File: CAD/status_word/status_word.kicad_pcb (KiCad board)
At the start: 2 copper layers, 70 x 39 mm, 49 parts, among them J1 Conn_01x26_Pin, U1 74HC161, U2 74HC109, U3 74HC157, U4 74HC157, U5 74HC245, U6 74HC02

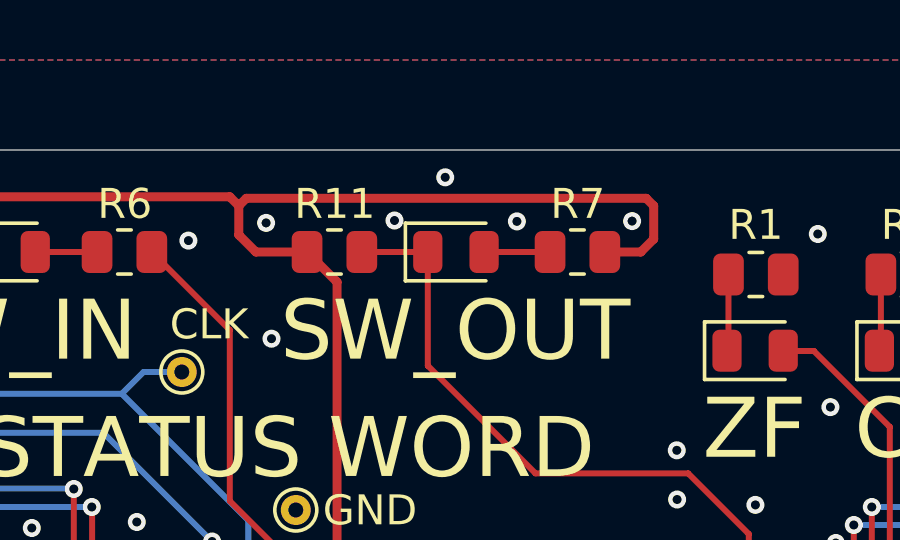
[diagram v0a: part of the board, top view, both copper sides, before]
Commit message: update SW, fix component rotations
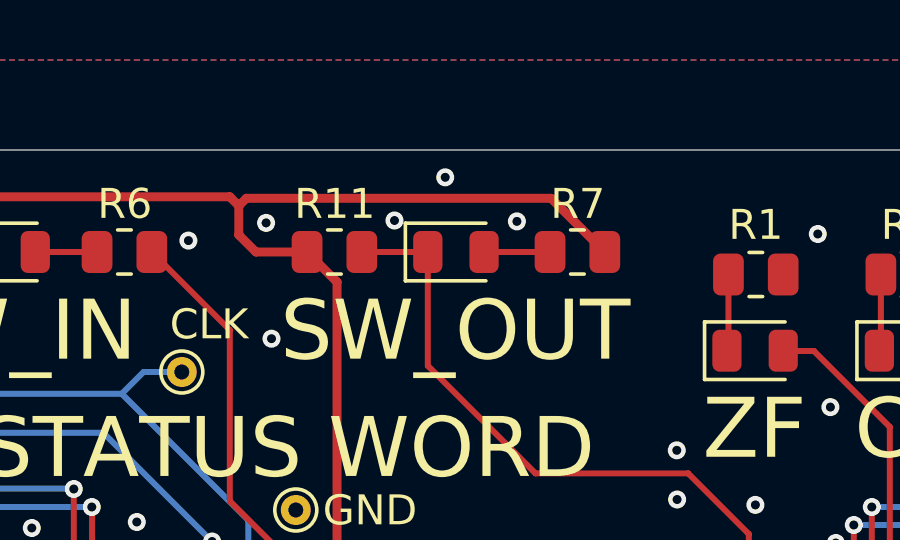
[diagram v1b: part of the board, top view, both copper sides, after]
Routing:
- net +5V: track 194.1 -> 190.2 mm
- net GND: vias 87 -> 86

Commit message: SW layout changes
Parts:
- TP2: moved to B.Cu
- turned TP2 to 180 degrees
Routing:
- net /sw.im: track 101.0 -> 100.0 mm
- net /sw.nf: track 84.3 -> 85.0 mm
- net /aflags.cf: track 27.6 -> 27.1 mm
- net /dbus3: track 62.6 -> 62.1 mm
- net GND: vias 86 -> 99

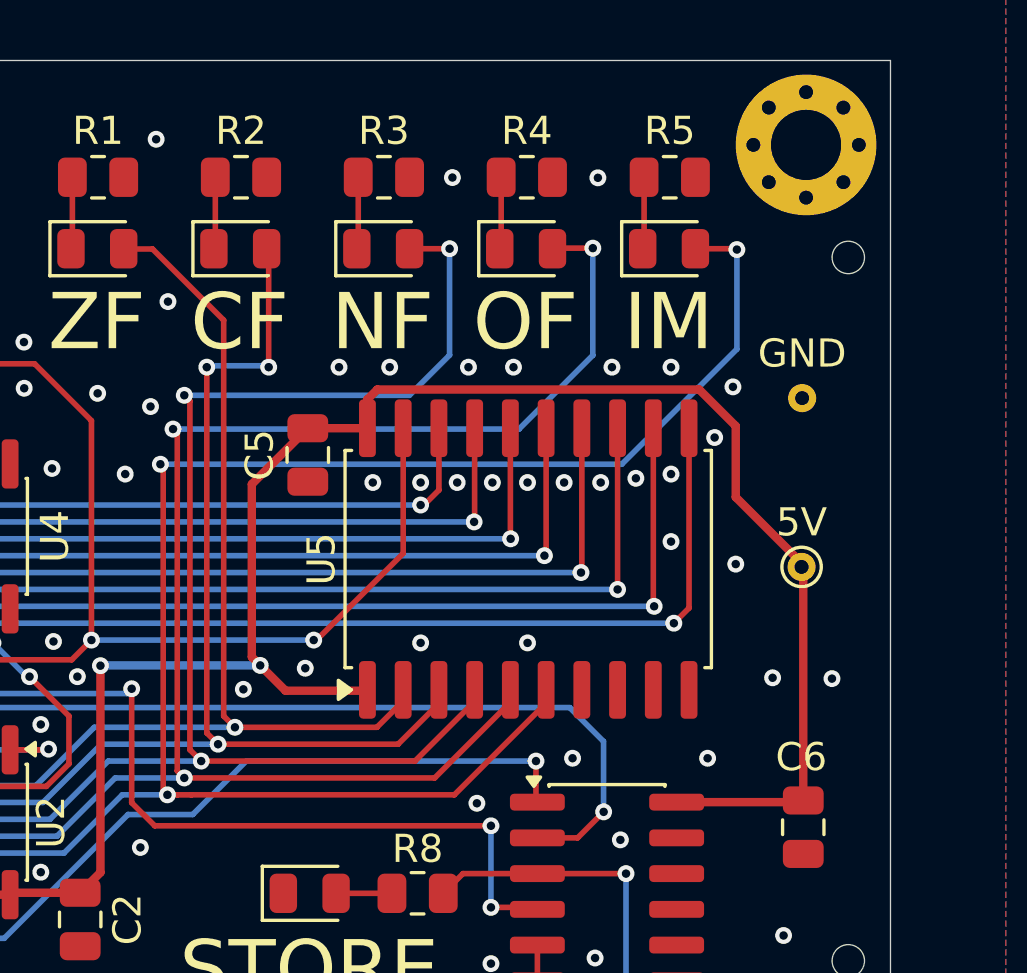
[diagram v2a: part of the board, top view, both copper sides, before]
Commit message: SW add keystone 5015 testpoint, small layout improvements
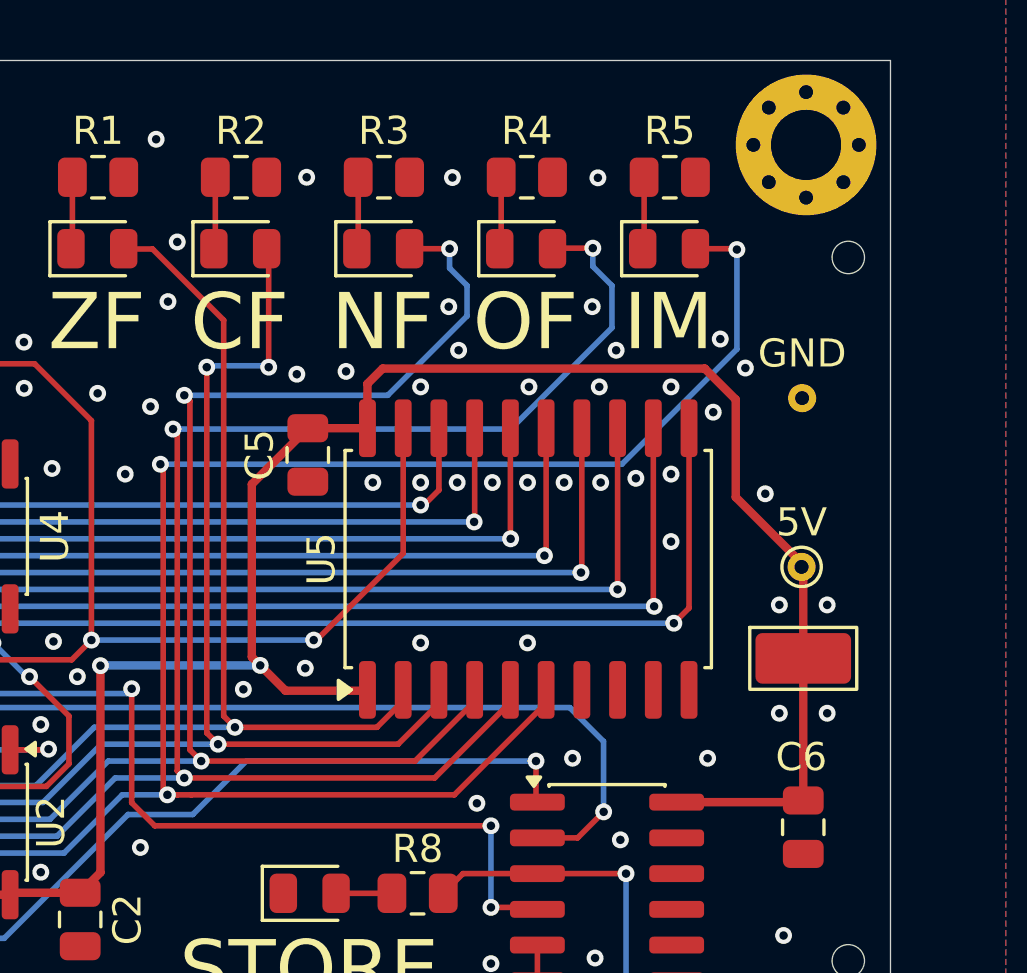
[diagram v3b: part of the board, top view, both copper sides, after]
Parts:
- added TP5: RH-5015, TestPoint:TestPoint_Keystone_5015_Micro_Mini, F.Cu at (120.9, 60.2)
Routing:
- net +5V: track 189.8 -> 191.4 mm
- net GND: vias 99 -> 108

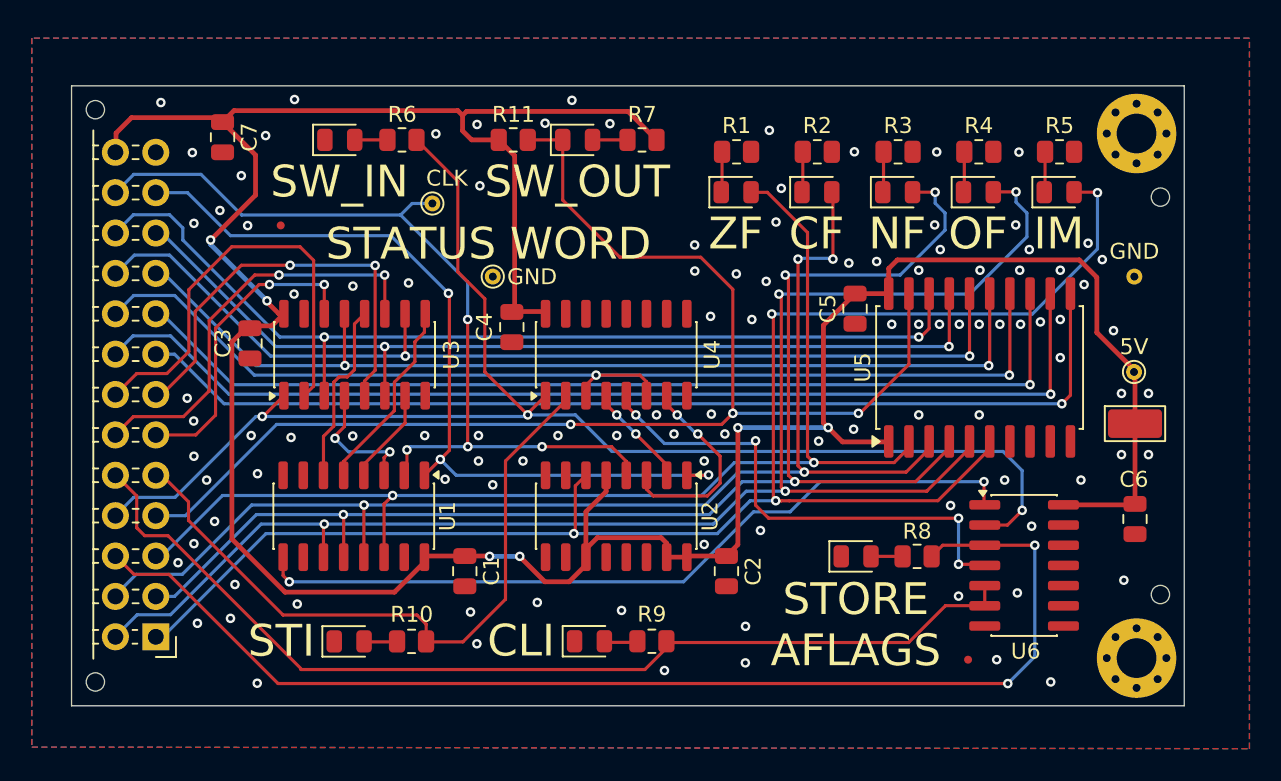
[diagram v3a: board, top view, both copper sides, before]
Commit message: rotation of RH5015 test point, small layout improvements
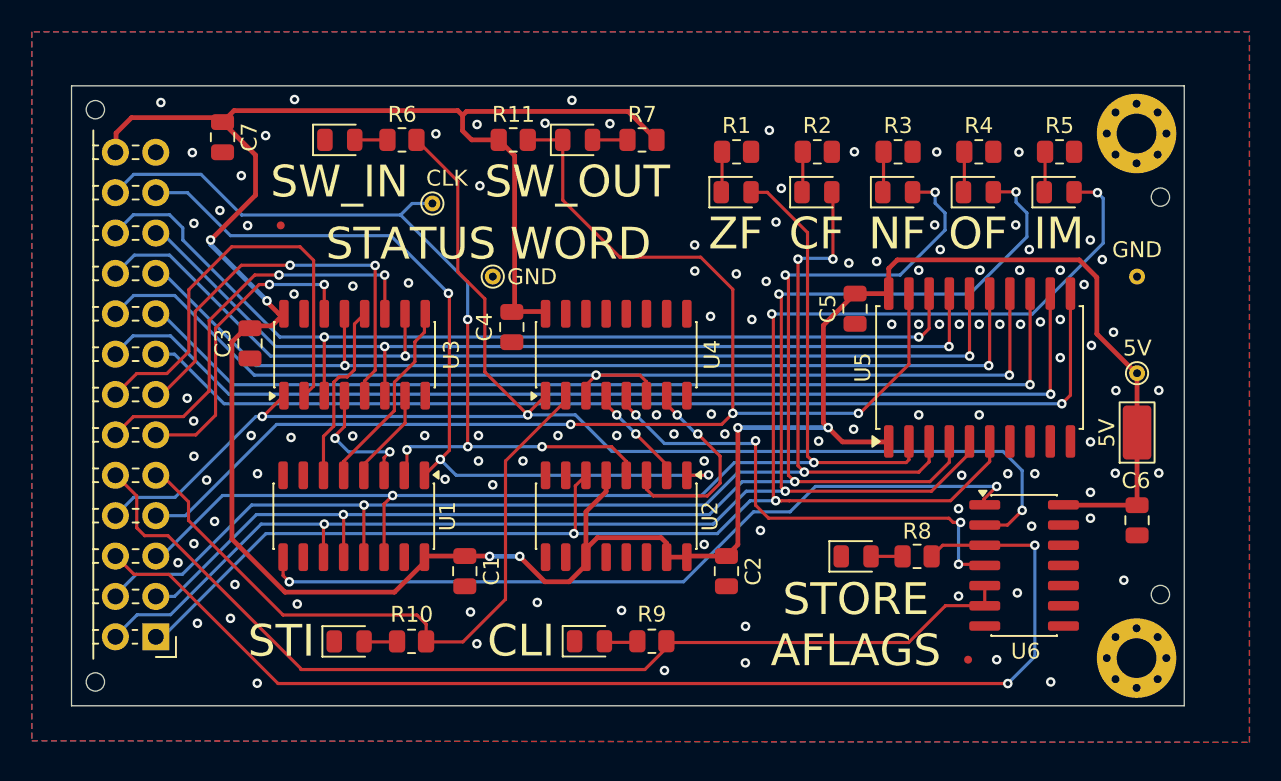
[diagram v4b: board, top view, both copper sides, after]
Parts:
- moved TP5 0.57 mm to (121.0, 60.8), turned to 90 degrees
- moved TP1 0.21 mm to (121.0, 57.1)
- moved TP2 0.17 mm to (121.0, 51.0)
- moved C6 0.15 mm to (121.0, 66.3)
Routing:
- net /sw.im: track 100.0 -> 100.7 mm
- net Net-(U1-~{PE}): track 49.4 -> 50.1 mm
- net /sw.nf: track 85.0 -> 85.5 mm
- net GND: vias 108 -> 113

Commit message: update KiCAD version 10.0
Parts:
- removed G***: LOGO, 8-bit_computer:qr-code-github
